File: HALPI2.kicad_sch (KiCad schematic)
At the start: 0 parts

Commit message: Fix schematic ERC errors
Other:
- sheet CM4 GPIO ports: added I2C1{I2C}; removed I2C{I2C}
- sheet Controller ports: added I2C1{I2C}, Vscap; removed I2C0{I2C}, Vcap
- sheet Power ports: added Vscap; removed Vcap

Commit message: Renumber all sheets
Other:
- sheet Controller ports: added none; removed RTC_INT

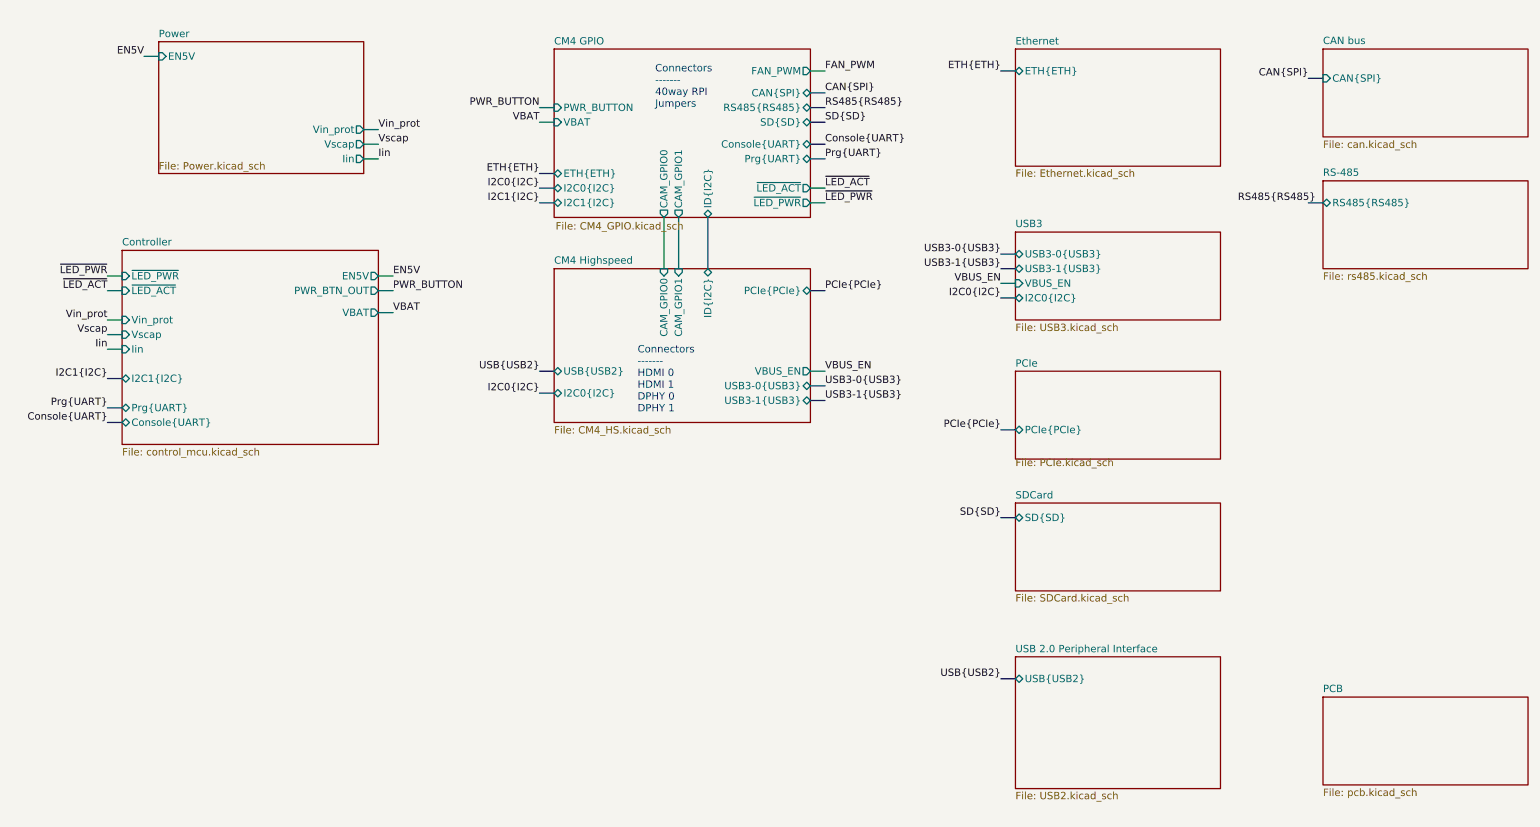
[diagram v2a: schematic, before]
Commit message: Most DRC errors fixed
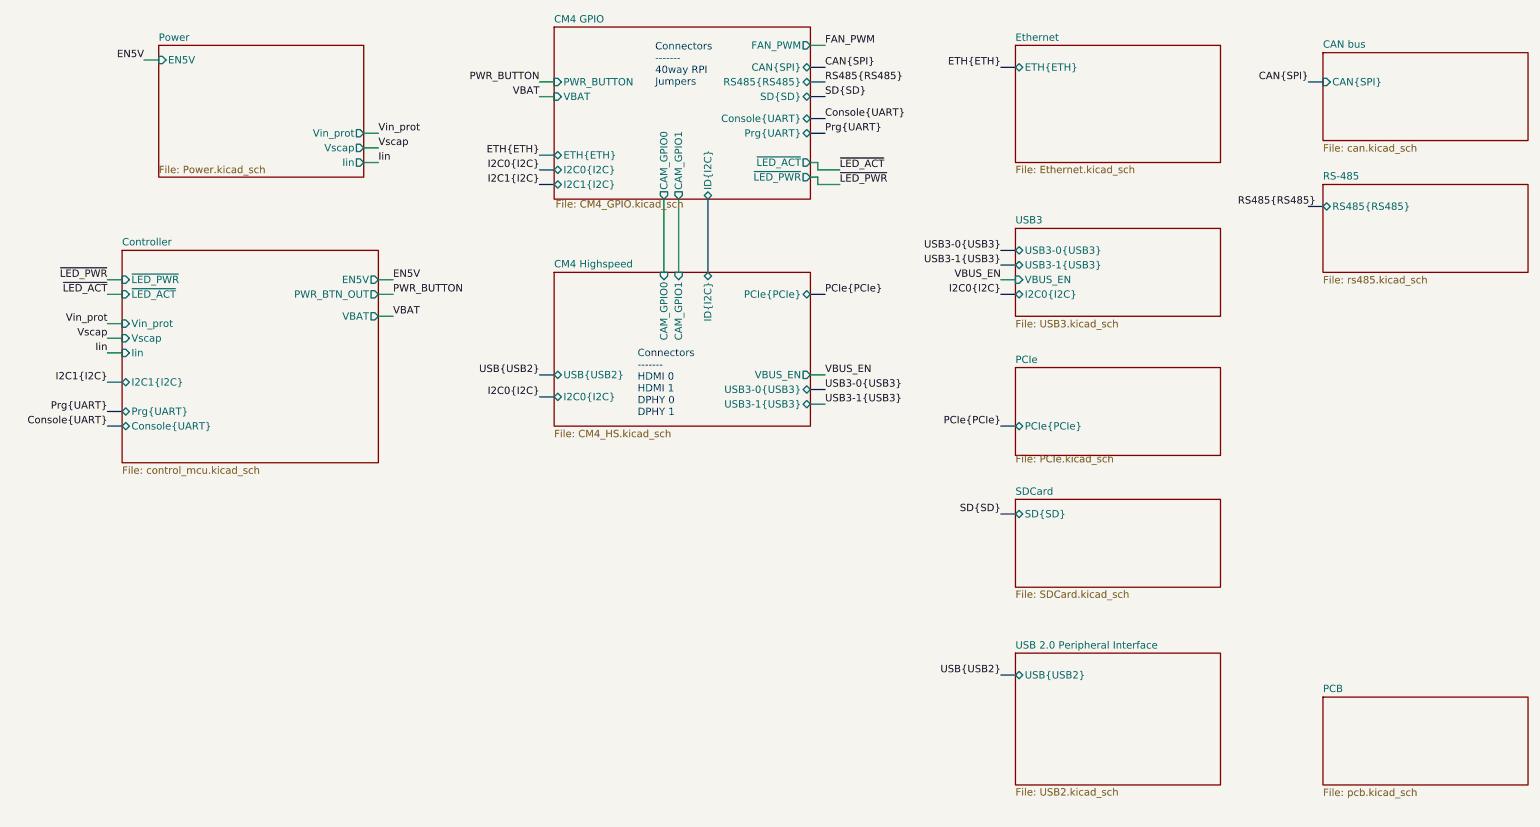
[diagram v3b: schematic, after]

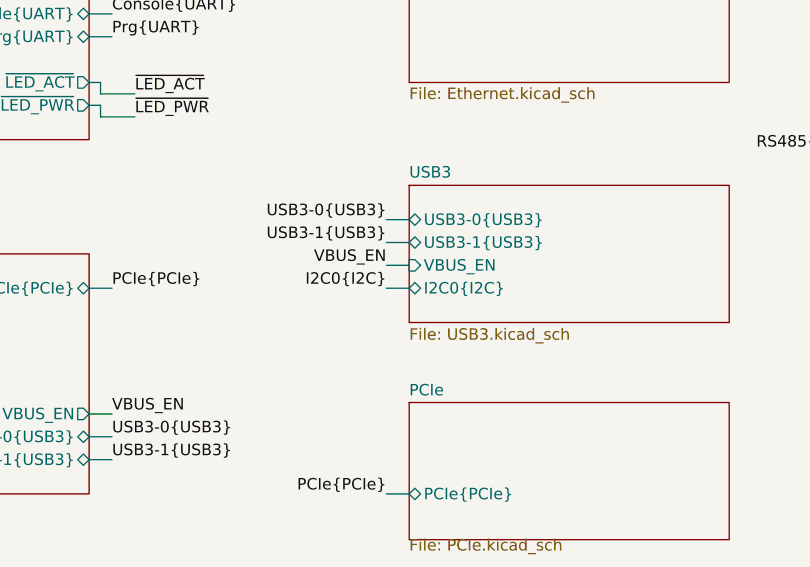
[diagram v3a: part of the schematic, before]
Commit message: Finish the board redesign with SoM on the bottom
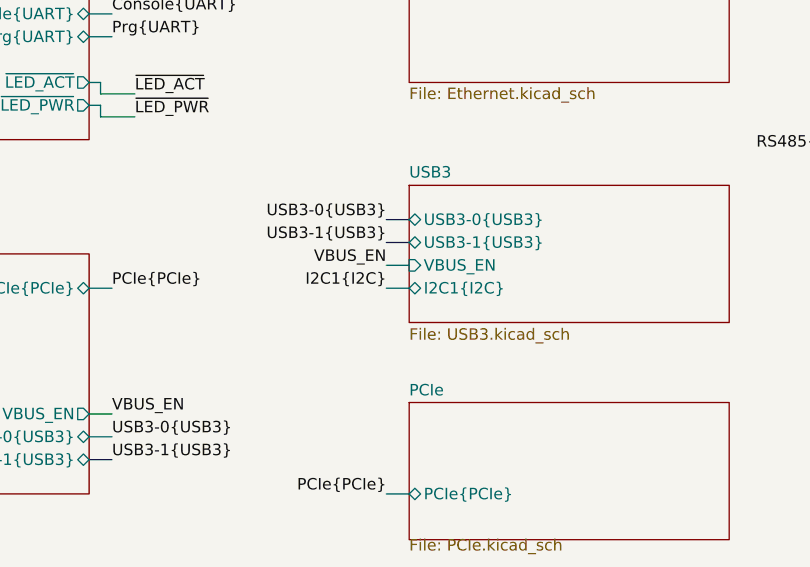
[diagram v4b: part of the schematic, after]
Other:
- sheet USB3 ports: added I2C1{I2C}; removed I2C0{I2C}
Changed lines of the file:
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@@
 		)
 	)
-	(label "I2C0{I2C}"
+	(label "I2C1{I2C}"
 		(at 184.15 66.04 180)
 		(effects
@@
 			)
 		)
-		(pin "I2C0{I2C}" bidirectional
+		(pin "I2C1{I2C}" bidirectional
 			(at 186.69 66.04 180)
 			(effects

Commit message: Further refinements
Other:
- sheet Controller ports: added VCCEN; removed EN5V
- sheet Power ports: added VCCEN; removed EN5V
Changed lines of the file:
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@@
 		)
 	)
-	(label "EN5V"
+	(label "VCCEN"
 		(at 35.56 25.4 180)
 		(effects
@@
 		)
 	)
-	(label "EN5V"
+	(label "VCCEN"
 		(at 78.74 63.5 0)
 		(effects
@@
 			)
 		)
-		(pin "EN5V" output
+		(pin "VCCEN" output
 			(at 76.2 63.5 0)
 			(effects
@@
 			)
 		)
-		(pin "EN5V" input
+		(pin "VCCEN" input
 			(at 38.1 25.4 180)
 			(effects

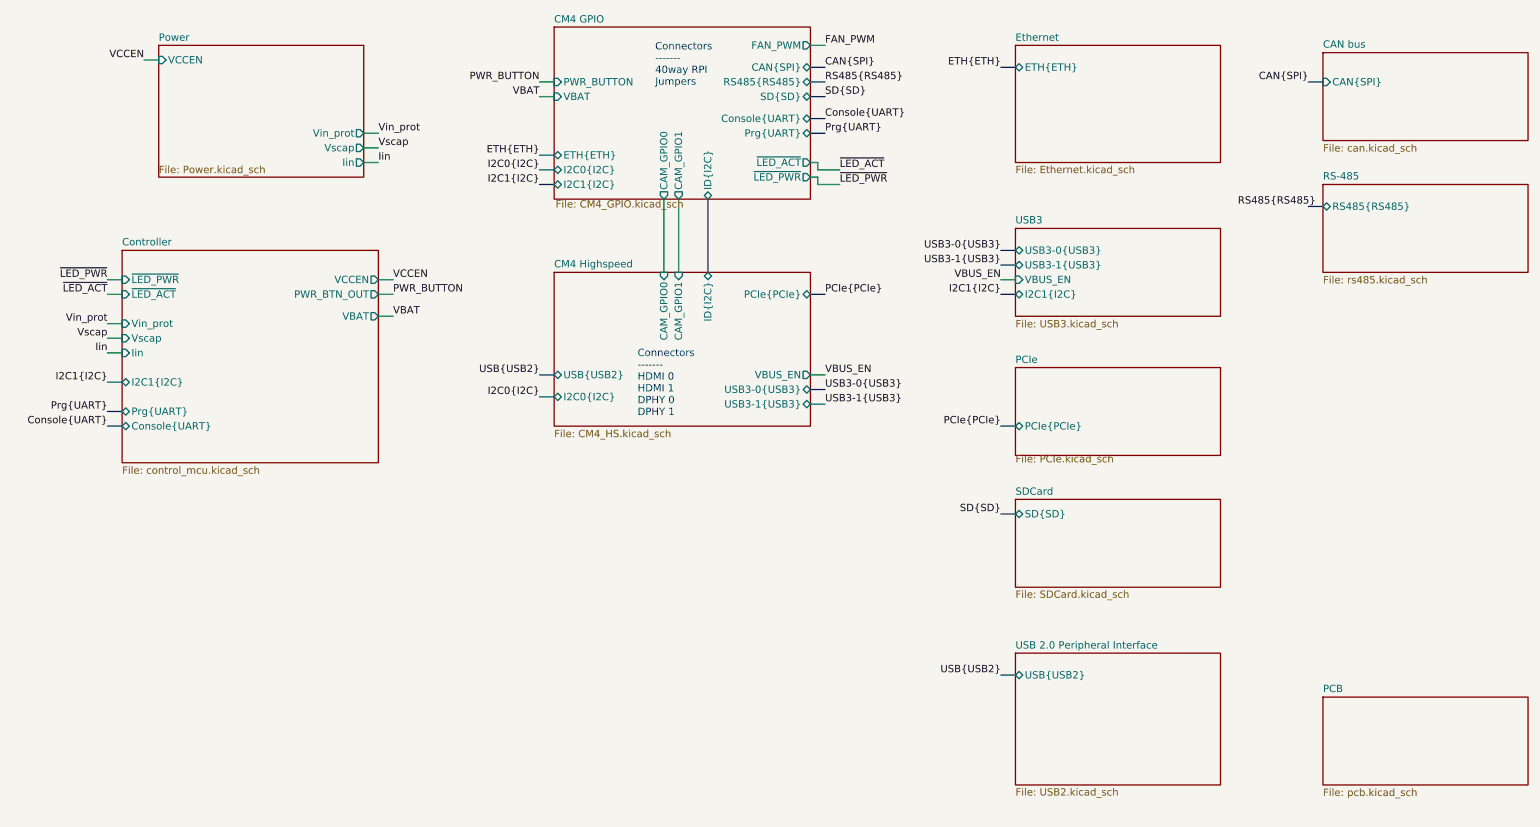
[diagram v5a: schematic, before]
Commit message: Change MCU to RP2040
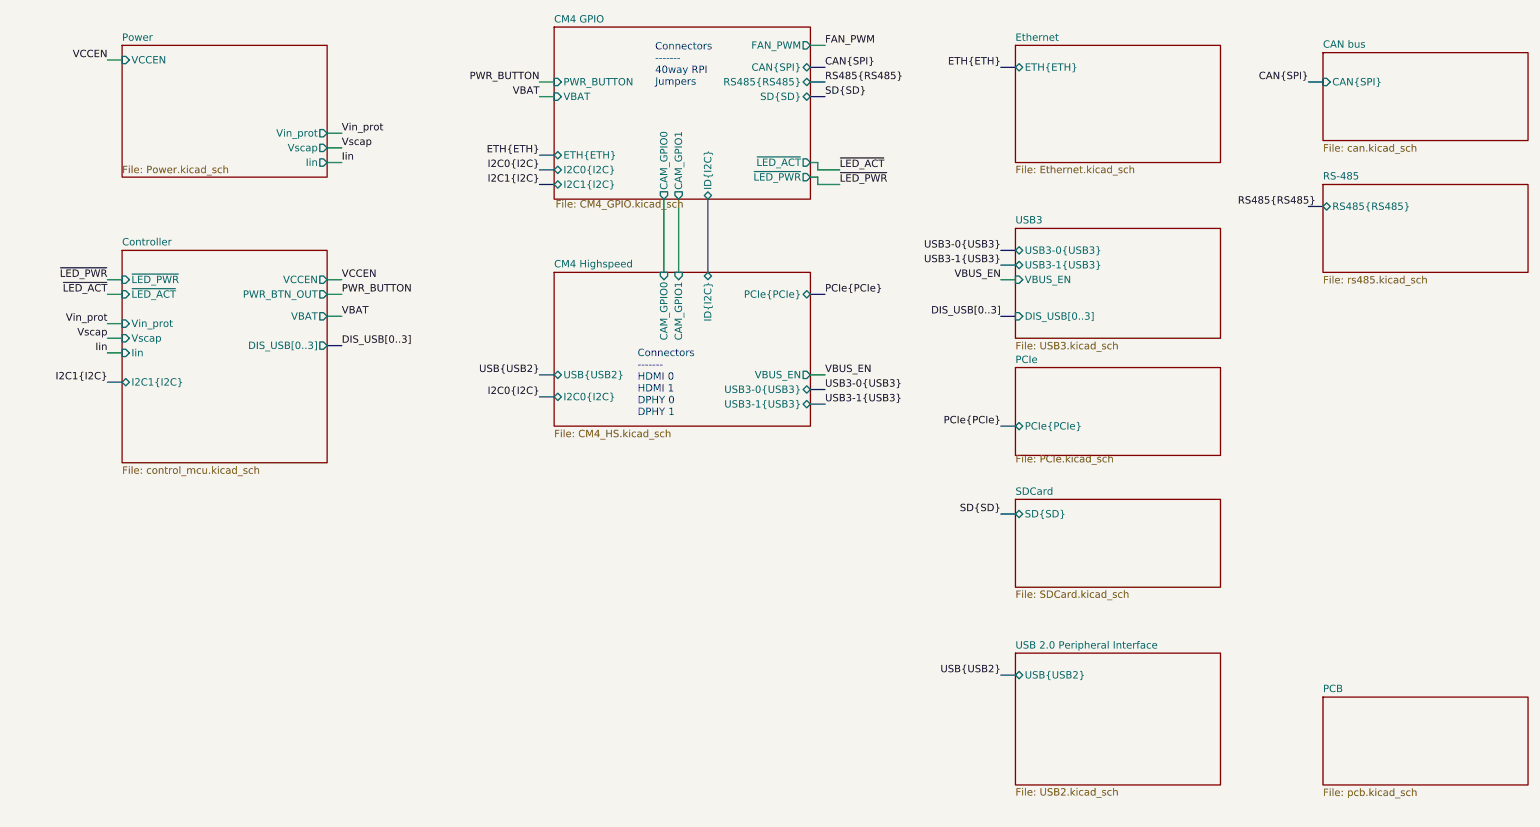
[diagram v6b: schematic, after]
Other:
- sheet CM4 GPIO ports: added none; removed Console{UART}, Prg{UART}
- sheet Controller ports: added DIS_USB[0..3]; removed Console{UART}, Prg{UART}
- sheet USB3 ports: added DIS_USB[0..3]; removed I2C1{I2C}
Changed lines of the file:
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@@
-	(bus
-		(pts
-			(xy 31.75 86.36) (xy 29.21 86.36)
-		)
-		(stroke
-			(width 0)
-			(type default)
-		)
-	)
 	(bus
 		(pts
@@
 		)
 	)
-	(bus
-		(pts
-			(xy 184.15 66.04) (xy 186.69 66.04)
-		)
-		(stroke
-			(width 0)
-			(type default)
-		)
-	)
 	(wire
 		(pts
@@
 		)
 	)
-	(bus
-		(pts
-			(xy 151.13 38.1) (xy 153.67 38.1)
-		)
-		(stroke
-			(width 0)
-			(type default)
-		)
-	)
 	(wire
 		(pts
@@
 	(wire
 		(pts
-			(xy 73.66 40.64) (xy 76.2 40.64)
+			(xy 67.31 40.64) (xy 69.85 40.64)
+		)
+		(stroke
+			(width 0)
+			(type default)
+		)
+	)
+	(bus
+		(pts
+			(xy 184.15 69.85) (xy 186.69 69.85)
 		)
 		(stroke
@@
 	(wire
 		(pts
-			(xy 38.1 25.4) (xy 35.56 25.4)
+			(xy 31.75 25.4) (xy 29.21 25.4)
 		)
 		(stroke
@@
 	(wire
 		(pts
-			(xy 73.66 38.1) (xy 76.2 38.1)
+			(xy 67.31 38.1) (xy 69.85 38.1)
+		)
+		(stroke
+			(width 0)
+			(type default)
+		)
+	)
+	(bus
+		(pts
+			(xy 69.85 74.93) (xy 67.31 74.93)
 		)
 		(stroke
@@
 	(wire
 		(pts
-			(xy 73.66 43.18) (xy 76.2 43.18)
+			(xy 67.31 43.18) (xy 69.85 43.18)
 		)
 		(stroke
@@
 	(wire
 		(pts
-			(xy 78.74 66.04) (xy 76.2 66.04)
+			(xy 69.85 66.04) (xy 67.31 66.04)
 		)
 		(stroke
@@
 	(wire
 		(pts
-			(xy 78.74 63.5) (xy 76.2 63.5)
+			(xy 69.85 63.5) (xy 67.31 63.5)
 		)
 		(stroke
@@
 		)
 	)
-	(bus
-		(pts
-			(xy 31.75 88.9) (xy 29.21 88.9)
-		)
-		(stroke
-			(width 0)
-			(type default)
-		)
-	)
 	(wire
 		(pts
@@
 	(wire
 		(pts
-			(xy 78.74 69.85) (xy 76.2 69.85)
+			(xy 69.85 69.85) (xy 67.31 69.85)
 		)
 		(stroke
@@
 	(bus
 		(pts
-			(xy 151.13 35.56) (xy 153.67 35.56)
-		)
-		(stroke
-			(width 0)
-			(type default)
-		)
-	)
-	(bus
-		(pts
 			(xy 104.14 83.82) (xy 106.68 83.82)
 		)
@@
 	)
 	(label "VCCEN"
-		(at 35.56 25.4 180)
+		(at 29.21 25.4 180)
 		(effects
 			(font
@@
 	)
 	(label "VCCEN"
-		(at 78.74 63.5 0)
+		(at 69.85 63.5 0)
 		(effects
 			(font
@@
 		)
 	)
-	(label "Console{UART}"
-		(at 29.21 88.9 180)
-		(effects
-			(font
-				(size 1.27 1.27)
-			)
-			(justify right bottom)
-		)
-	)
 	(label "Iin"
-		(at 76.2 43.18 0)
+		(at 69.85 43.18 0)
 		(effects
 			(font
@@
 	)
 	(label "VBAT"
-		(at 78.74 69.85 0)
+		(at 69.85 69.85 0)
 		(effects
 			(font
@@
 		)
 	)
-	(label "Console{UART}"
-		(at 153.67 35.56 0)
-		(effects
-			(font
-				(size 1.27 1.27)
-			)
-			(justify left bottom)
-		)
-	)
 	(label "VBAT"
 		(at 104.14 31.75 180)
@@
 		)
 	)
+	(label "DIS_USB[0..3]"
+		(at 184.15 69.85 180)
+		(effects
+			(font
+				(size 1.27 1.27)
+			)
+			(justify right bottom)
+		)
+	)
 	(label "ETH{ETH}"
 		(at 104.14 41.91 180)
@@
 		)
 	)
-	(label "Prg{UART}"
-		(at 153.67 38.1 0)
-		(effects
-			(font
-				(size 1.27 1.27)
-			)
-			(justify left bottom)
-		)
-	)
 	(label "USB3-0{USB3}"
 		(at 184.15 58.42 180)
@@
 	)
 	(label "Vscap"
-		(at 76.2 40.64 0)
+		(at 69.85 40.64 0)
 		(effects
 			(font
@@
 	)
 	(label "PWR_BUTTON"
-		(at 78.74 66.04 0)
+		(at 69.85 66.04 0)
 		(effects
 			(font
@@
 		)
 	)
-	(label "Prg{UART}"
-		(at 29.21 86.36 180)
-		(effects
-			(font
-				(size 1.27 1.27)
-			)
-			(justify right bottom)
-		)
-	)
 	(label "Vin_prot"
-		(at 76.2 38.1 0)
+		(at 69.85 38.1 0)
 		(effects
 			(font
@@
 		)
 	)
+	(label "DIS_USB[0..3]"
+		(at 69.85 74.93 0)
+		(effects
+			(font
+				(size 1.27 1.27)
+			)
+			(justify left bottom)
+		)
+	)
 	(label "I2C1{I2C}"
 		(at 104.14 46.99 180)
@@
 	(label "ETH{ETH}"
 		(at 184.15 26.67 180)
-		(effects
-			(font
-				(size 1.27 1.27)
-			)
-			(justify right bottom)
-		)
-	)
-	(label "I2C1{I2C}"
-		(at 184.15 66.04 180)
 		(effects
 			(font
@@
 			)
 		)
-		(pin "Console{UART}" bidirectional
-			(at 151.13 35.56 0)
-			(effects
-				(font
-					(size 1.27 1.27)
-				)
-				(justify right)
-			)
-		)
-		(pin "Prg{UART}" bidirectional
-			(at 151.13 38.1 0)
-			(effects
-				(font
-					(size 1.27 1.27)
-				)
-				(justify right)
-			)
-		)
 		(pin "RS485{RS485}" bidirectional
 			(at 151.13 29.21 0)
@@
 	(sheet
 		(at 31.75 58.42)
-		(size 44.45 36.83)
+		(size 35.56 36.83)
 		(exclude_from_sim no)
 		(in_bom yes)
@@
 			)
 		)
-		(pin "Prg{UART}" bidirectional
-			(at 31.75 86.36 180)
-			(effects
-				(font
-					(size 1.27 1.27)
-				)
-				(justify left)
-			)
-		)
-		(pin "Console{UART}" bidirectional
-			(at 31.75 88.9 180)
-			(effects
-				(font
-					(size 1.27 1.27)
-				)
-				(justify left)
-			)
-		)
 		(pin "Vin_prot" input
 			(at 31.75 71.12 180)
@@
 		)
 		(pin "VCCEN" output
-			(at 76.2 63.5 0)
+			(at 67.31 63.5 0)
 			(effects
 				(font
@@
 		)
 		(pin "PWR_BTN_OUT" output
-			(at 76.2 66.04 0)
+			(at 67.31 66.04 0)
 			(effects
 				(font
@@
 		)
 		(pin "VBAT" output
-			(at 76.2 69.85 0)
+			(at 67.31 69.85 0)
 			(effects
 				(font
@@
 				)
 				(justify left)
+			)
+		)
+		(pin "DIS_USB[0..3]" output
+			(at 67.31 74.93 0)
+			(effects
+				(font
+					(size 1.27 1.27)
+				)
+				(justify right)
 			)
 		)
@@
 	(sheet
 		(at 186.69 54.61)
-		(size 35.56 15.24)
+		(size 35.56 19.05)
 		(exclude_from_sim no)
 		(in_bom yes)
@@
 		)
 		(property "Sheetfile" "USB3.kicad_sch"
-			(at 186.69 70.4346 0)
+			(at 186.69 74.2446 0)
 			(effects
 				(font
@@
 			)
 		)
-		(pin "I2C1{I2C}" bidirectional
-			(at 186.69 66.04 180)
+		(pin "DIS_USB[0..3]" input
+			(at 186.69 69.85 180)
 			(effects
 				(font
@@
 	)
 	(sheet
-		(at 38.1 22.86)
+		(at 31.75 22.86)
 		(size 35.56 22.86)
 		(exclude_from_sim no)
@@
 		)
 		(property "Sheetname" "Power"
-			(at 38.1 22.2241 0)
+			(at 31.75 22.2241 0)
 			(effects
 				(font
@@
 		)
 		(property "Sheetfile" "Power.kicad_sch"
-			(at 38.1 43.6889 0)
+			(at 31.75 43.6889 0)
 			(effects
 				(font
@@
 		)
 		(pin "Iin" output
-			(at 73.66 43.18 0)
+			(at 67.31 43.18 0)
 			(effects
 				(font
@@
 		)
 		(pin "VCCEN" input
-			(at 38.1 25.4 180)
+			(at 31.75 25.4 180)
 			(effects
 				(font
@@
 		)
 		(pin "Vscap" output
-			(at 73.66 40.64 0)
+			(at 67.31 40.64 0)
 			(effects
 				(font
@@
 		)
 		(pin "Vin_prot" output
-			(at 73.66 38.1 0)
-			(effects
-				(font
+			(at 67.31 38.1 0)
+			(effects
+				(font

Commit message: Finish transitioning to RP2040
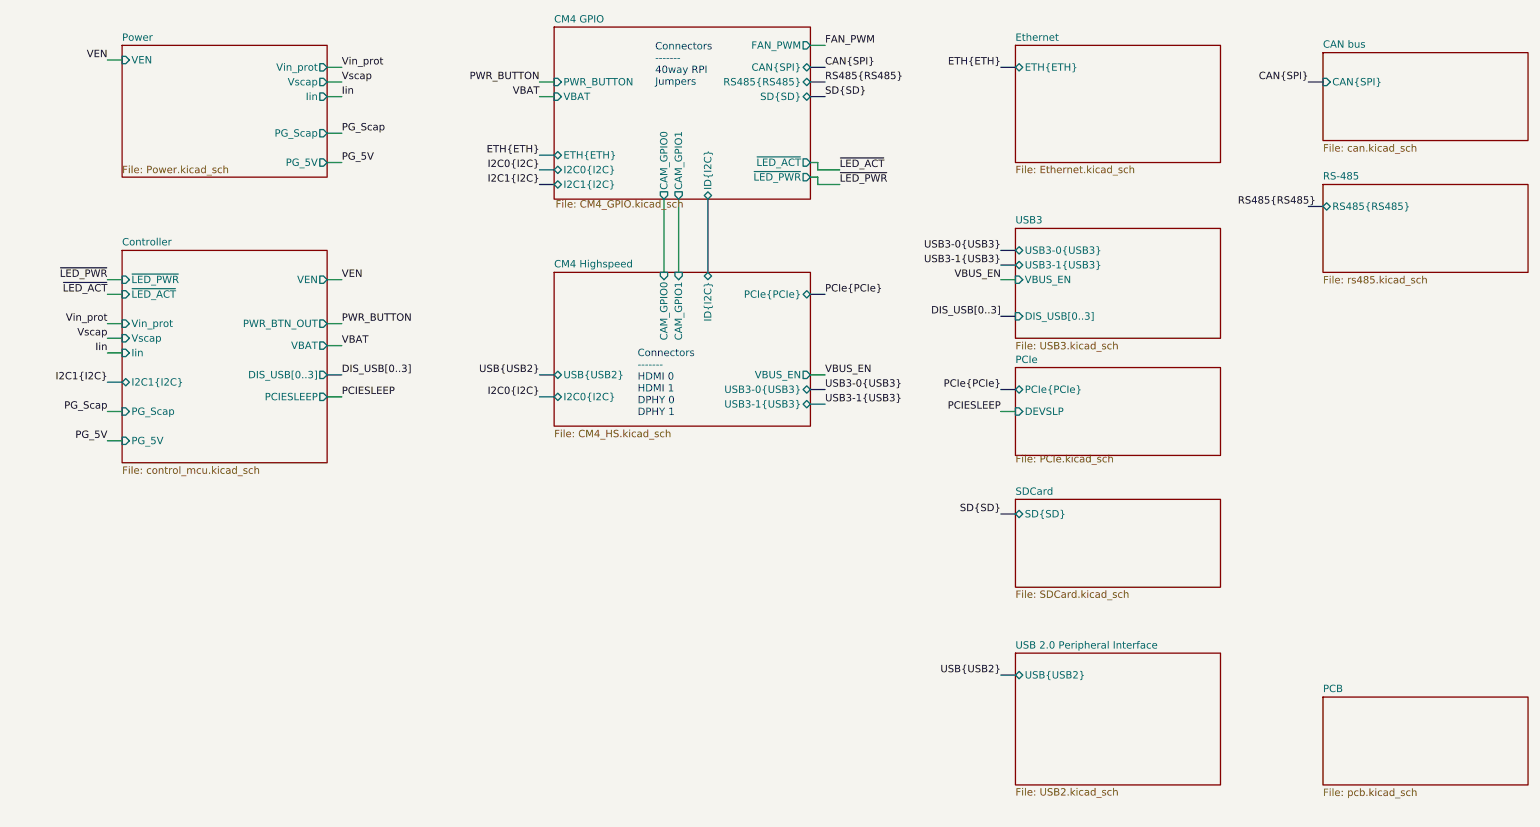
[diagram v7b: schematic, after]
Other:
- sheet Controller ports: added PCIESLEEP, PG_5V, PG_Scap, VEN; removed VCCEN
- sheet PCIe ports: added DEVSLP; removed none
- sheet Power ports: added PG_5V, PG_Scap, VEN; removed VCCEN
